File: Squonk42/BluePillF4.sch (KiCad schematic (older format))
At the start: 59 parts, among them J1 MH20-1, J2 MH20-1, J3 MH_RA4-1, J4 MR07C-06200, J5 U02-BFD3111B0-009, U1 AP2114HA-3.3TRG1, U2 AP2112K3.3-TRG1, U3 STM32F405RGT6, U4 SY6280, Y1 FC-12M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

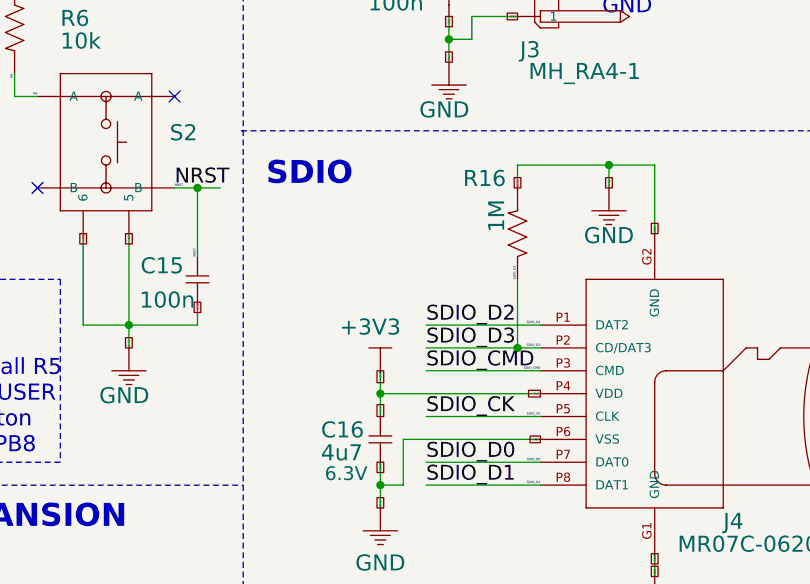
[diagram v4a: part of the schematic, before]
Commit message: Added inductor on SDIO_VDD to prevent transcient upon hot SDCard insertion
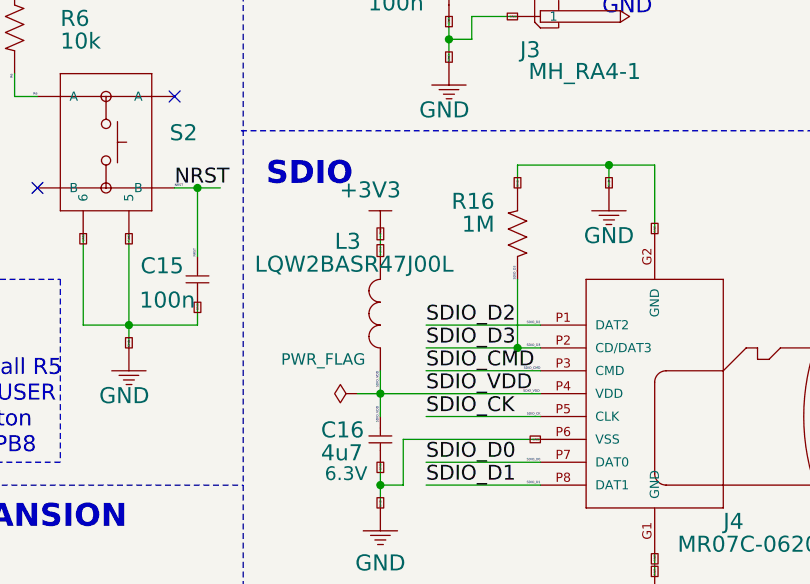
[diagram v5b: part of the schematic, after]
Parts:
- added L3: LQW2BASR47J00L, BluePillF4 Lib:FB0805, symbol FB_0805
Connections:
- net labels added: SDIO_VDD
- wire segments 269 -> 270
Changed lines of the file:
@@
 Sheet 1 1
 Title "BluePill F4"
-Date "2017-12-27"
+Date "2017-12-28"
 Rev "A"
 Comp "© 2017 www.stm32duino.com, All rights reserved."
@@
 L +3V3 #SUPPLY030
 U 1 1 5A08C09A
-P 9100 2700
-F 0 "#SUPPLY030" H 9100 2850 70  0001 L BNN
-F 1 "+3V3" H 9010 2850 70  0000 L BNN
-F 2 "" H 9100 2700 60  0001 C CNN
-F 3 "" H 9100 2700 60  0001 C CNN
-	1    9100 2700
+P 9100 2100
+F 0 "#SUPPLY030" H 9100 2250 70  0001 L BNN
+F 1 "+3V3" H 9010 2250 70  0000 L BNN
+F 2 "" H 9100 2100 60  0001 C CNN
+F 3 "" H 9100 2100 60  0001 C CNN
+	1    9100 2100
 	-1   0    0    -1
 $EndComp
@@
 Text GLabel 2400 1100 3    10   UnSpc ~ 0
 +3V3
-Text GLabel 9100 2700 3    10   UnSpc ~ 0
-+3V3
-Text GLabel 9100 2900 1    10   UnSpc ~ 0
-+3V3
-Text GLabel 9800 2800 0    10   UnSpc ~ 0
-+3V3
 Text GLabel 3300 3500 1    10   UnSpc ~ 0
 +3V3
@@
 Connection ~ 2400 1200
 Wire Wire Line
-	9100 2800 9800 2800
-Wire Wire Line
-	9100 2700 9100 2900
-Connection ~ 9100 2800
-Wire Wire Line
 	3300 2800 3300 3500
 Wire Wire Line
@@
 U 1 1 5A42D7B9
 P 9700 2100
-F 0 "R16" V 9900 2050 70  0000 R TNN
-F 1 "1M" H 9850 2050 70  0000 R TNN
+F 0 "R16" V 9800 2000 70  0000 R TNN
+F 1 "1M" V 9700 2000 70  0000 R TNN
 F 2 "BluePillF4 Lib:R0603" H 9690 1890 65  0001 L TNN
 F 3 "" H 9700 2100 60  0001 C CNN
@@
 Text Label 9700 2300 1    10   ~ 0
 SDIO_D3
+$Comp
+L FB_0805 L3
+U 1 1 5A44FA55
+P 9100 2500
+F 0 "L3" V 9425 2700 70  0000 R TNN
+F 1 "LQW2BASR47J00L" V 9325 3050 70  0000 R TNN
+F 2 "BluePillF4 Lib:FB0805" H 9130 2650 20  0001 C CNN
+F 3 "http://search.murata.co.jp/Ceramy/image/img/P02/JELF243A-0084.pdf" H 9100 2500 60  0001 C CNN
+F 4 "LQW2BASR47J00L" H 9100 2500 60  0001 C CNN "PARTNO"
+F 5 "0805" H 9100 2500 60  0001 C CNN "SIZE"
+F 6 "250mA" H 9100 2500 60  0001 C CNN "RATE"
+F 7 "F" H 9100 2500 60  0001 C CNN "DNP"
+	1    9100 2500
+	0    -1   -1   0
+$EndComp
+Wire Wire Line
+	9000 2800 9800 2800
+Wire Wire Line
+	9100 2700 9100 2900
+Connection ~ 9100 2800
+Wire Wire Line
+	9100 2200 9100 2100
+Text GLabel 9100 2075 3    10   UnSpc ~ 0
++3V3
+Text GLabel 9100 2200 1    10   UnSpc ~ 0
++3V3
+Text Label 9725 2800 0    10   ~ 0
+SDIO_VDD
+Text Label 9100 2700 3    10   ~ 0
+SDIO_VDD
+Text Label 9100 2925 1    10   ~ 0
+SDIO_VDD
+Text Label 9300 2800 0    65   ~ 0
+SDIO_VDD
+$Comp
+L PWR_FLAG #FLG048
+U 1 1 5A452CF2
+P 9000 2800
+F 0 "#FLG048" H 9000 2875 50  0001 C CNN
+F 1 "PWR_FLAG" V 9150 2950 50  0000 C CNN
+F 2 "" H 9000 2800 50  0001 C CNN
+F 3 "" H 9000 2800 50  0001 C CNN
+	1    9000 2800
+	0    -1   -1   0
+$EndComp
 $EndSCHEMATC
